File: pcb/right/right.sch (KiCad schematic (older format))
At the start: 127 parts, among them SW1 SW_Push, SW10 SW_Push, SW11 SW_Push, SW12 SW_Push, SW13 SW_Push, SW14 SW_Push, SW15 SW_Push, SW16 SW_Push, SW17 SW_Push, SW18 SW_Push, SW19 SW_Push, SW2 SW_Push, SW20 SW_Push, SW21 SW_Push, SW22 SW_Push, SW23 SW_Push, SW24 SW_Push, SW25 SW_Push, SW26 SW_Push, SW27 SW_Push, SW28 SW_Push, SW29 SW_Push, SW3 SW_Push, SW30 SW_Push, SW31 SW_Push, SW32 SW_Push, SW33 SW_Push, SW34 SW_Push, SW35 SW_Push, SW36 SW_Push, SW37 SW_Push, SW38 SW_Push, SW39 SW_Push, SW4 SW_Push, SW40 SW_Push, SW41 SW_Push, SW42 SW_Push, SW43 SW_Push, SW44 SW_Push, SW45 SW_Push, SW46 SW_Push, SW47 SW_Push, SW48 SW_Push, SW49 SW_Push, SW5 SW_Push, SW50 SW_Push, SW51 SW_Push, SW52 SW_Push, SW6 SW_Push, SW7 SW_Push, SW8 SW_Push, SW9 SW_Push

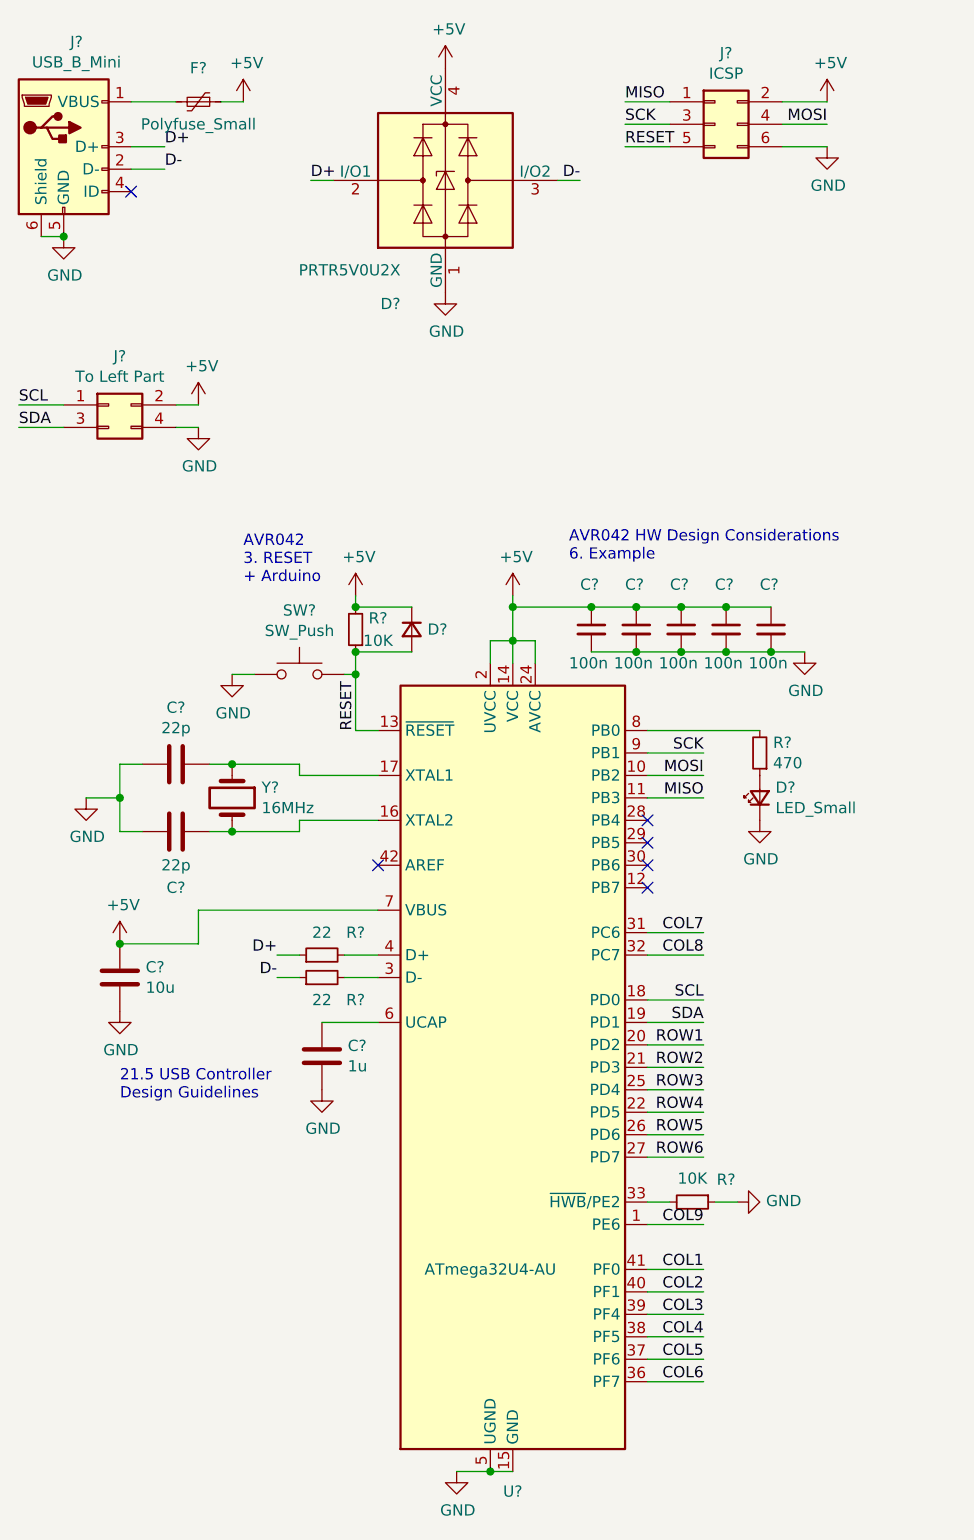
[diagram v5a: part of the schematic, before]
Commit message: pcb: right: annotate
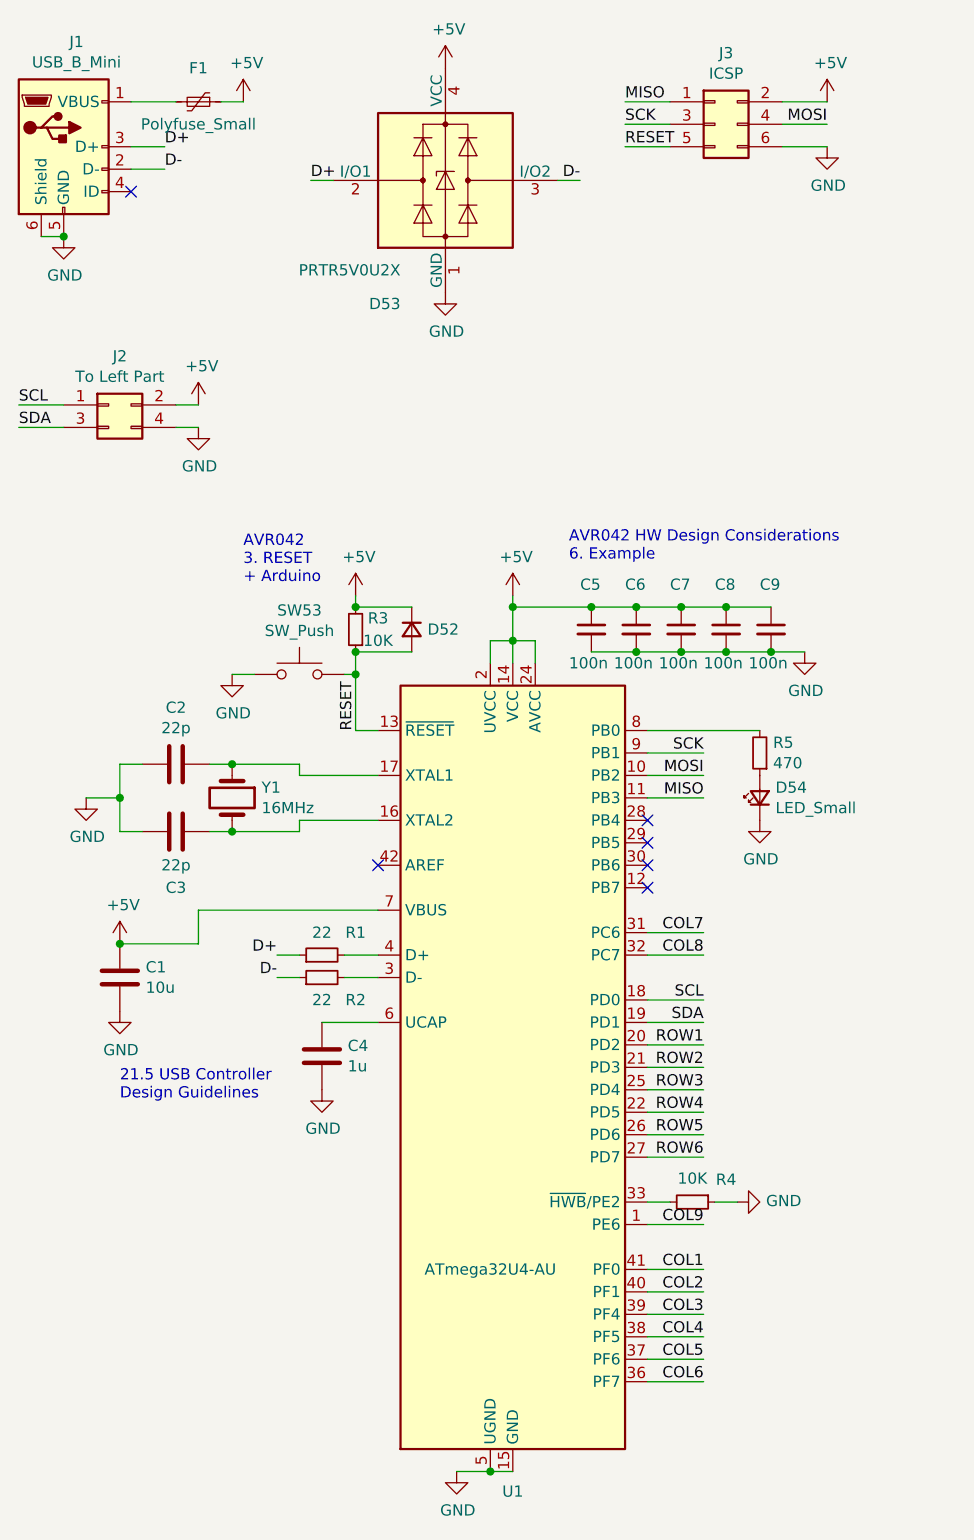
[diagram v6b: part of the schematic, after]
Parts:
- gave numbers to parts that had none: 24

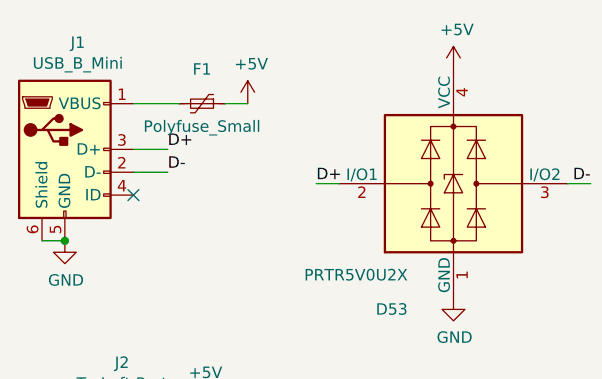
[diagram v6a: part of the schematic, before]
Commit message: pcb: right: PWR_FLAG for EDC
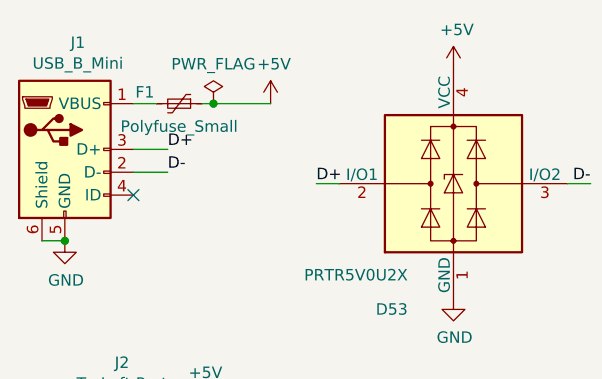
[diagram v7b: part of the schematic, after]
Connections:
- wire segments 208 -> 209
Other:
- moved on the sheet: F1
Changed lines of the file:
@@
 L Device:Polyfuse_Small F1
 U 1 1 603C544E
-P 1450 900
-F 0 "F1" V 1300 900 50  0000 C CNN
-F 1 "Polyfuse_Small" V 1550 900 50  0000 C CNN
-F 2 "" H 1500 700 50  0001 L CNN
-F 3 "~" H 1450 900 50  0001 C CNN
-	1    1450 900
+P 1350 900
+F 0 "F1" V 1300 750 50  0000 C CNN
+F 1 "Polyfuse_Small" V 1450 900 50  0000 C CNN
+F 2 "" H 1400 700 50  0001 L CNN
+F 3 "~" H 1350 900 50  0001 C CNN
+	1    1350 900
 	0    1    1    0
 $EndComp
@@
 Text Label 3150 1250 2    50   ~ 0
 D-
-Wire Wire Line
-	1150 900  1350 900
 $Comp
 L power:+5V #PWR0104
 U 1 1 6048134A
-P 1650 900
-F 0 "#PWR0104" H 1650 750 50  0001 C CNN
-F 1 "+5V" H 1665 1073 50  0000 C CNN
-F 2 "" H 1650 900 50  0001 C CNN
-F 3 "" H 1650 900 50  0001 C CNN
-	1    1650 900
-	1    0    0    -1
-$EndComp
-Wire Wire Line
-	1550 900  1650 900
+P 1750 900
+F 0 "#PWR0104" H 1750 750 50  0001 C CNN
+F 1 "+5V" H 1765 1073 50  0000 C CNN
+F 2 "" H 1750 900 50  0001 C CNN
+F 3 "" H 1750 900 50  0001 C CNN
+	1    1750 900
+	1    0    0    -1
+$EndComp
+Wire Wire Line
+	1450 900  1500 900
 $Comp
 L power:+5V #PWR0105
@@
 NoConn ~ 3450 4300
 NoConn ~ 3450 4400
+Wire Wire Line
+	1150 900  1250 900
+$Comp
+L power:PWR_FLAG #FLG0101
+U 1 1 604021BA
+P 1500 900
+F 0 "#FLG0101" H 1500 975 50  0001 C CNN
+F 1 "PWR_FLAG" H 1500 1073 50  0000 C CNN
+F 2 "" H 1500 900 50  0001 C CNN
+F 3 "~" H 1500 900 50  0001 C CNN
+	1    1500 900
+	1    0    0    -1
+$EndComp
+Connection ~ 1500 900
+Wire Wire Line
+	1500 900  1750 900
 $EndSCHEMATC

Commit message: pcb: right: Footprint for ICSP and left part connector
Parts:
- J2: footprint (none) -> Connector_PinHeader_2.54mm:PinHeader_2x02_P2.54mm_Vertical
- J3: footprint (none) -> Connector_PinHeader_2.54mm:PinHeader_2x03_P2.54mm_Vertical
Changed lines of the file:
@@
 F 0 "J3" H 3800 1317 50  0000 C CNN
 F 1 "ICSP" H 3800 1226 50  0000 C CNN
-F 2 "" H 3750 1000 50  0001 C CNN
+F 2 "Connector_PinHeader_2.54mm:PinHeader_2x03_P2.54mm_Vertical" H 3750 1000 50  0001 C CNN
 F 3 "~" H 3750 1000 50  0001 C CNN
 	1    3750 1000
@@
 F 0 "J2" H 1100 2467 50  0000 C CNN
 F 1 "To Left Part" H 1100 2376 50  0000 C CNN
-F 2 "" H 1050 2250 50  0001 C CNN
+F 2 "Connector_PinHeader_2.54mm:PinHeader_2x02_P2.54mm_Vertical" H 1050 2250 50  0001 C CNN
 F 3 "~" H 1050 2250 50  0001 C CNN
 	1    1050 2250
